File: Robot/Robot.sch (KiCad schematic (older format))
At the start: 3 parts

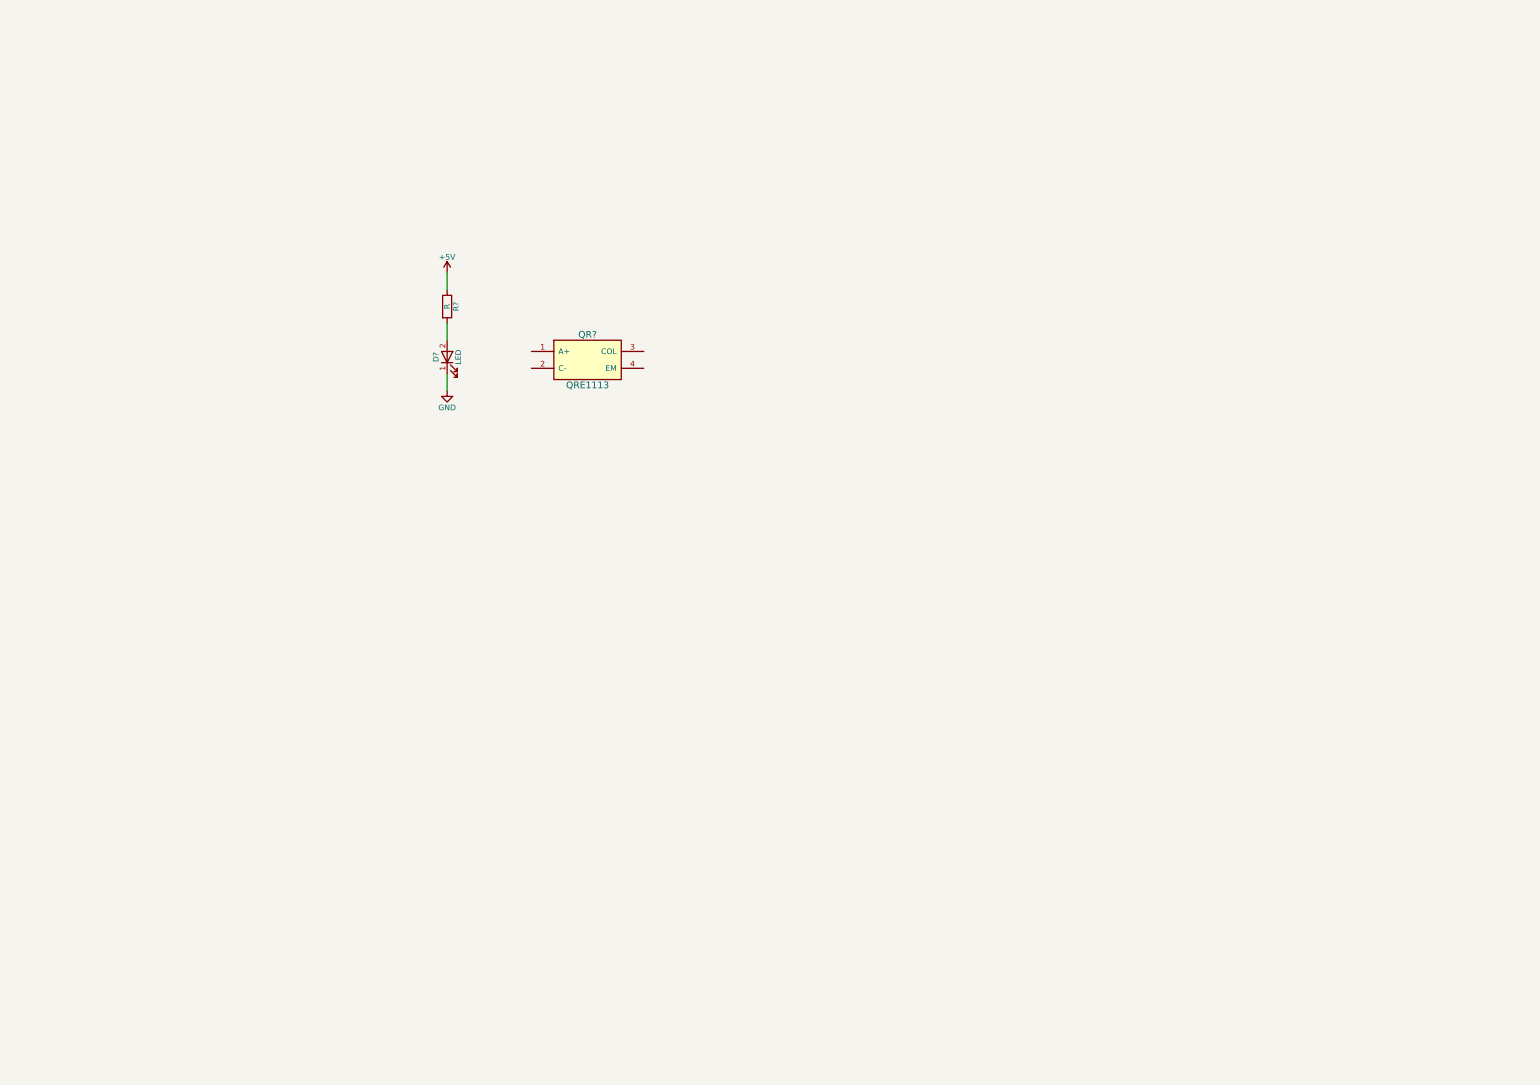
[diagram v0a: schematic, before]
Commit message: Dopolnjena shema za robot.
Dodan krmilnik, senzorji QRE1113, MUX, driver za motorje in enkoderji za
motorje.
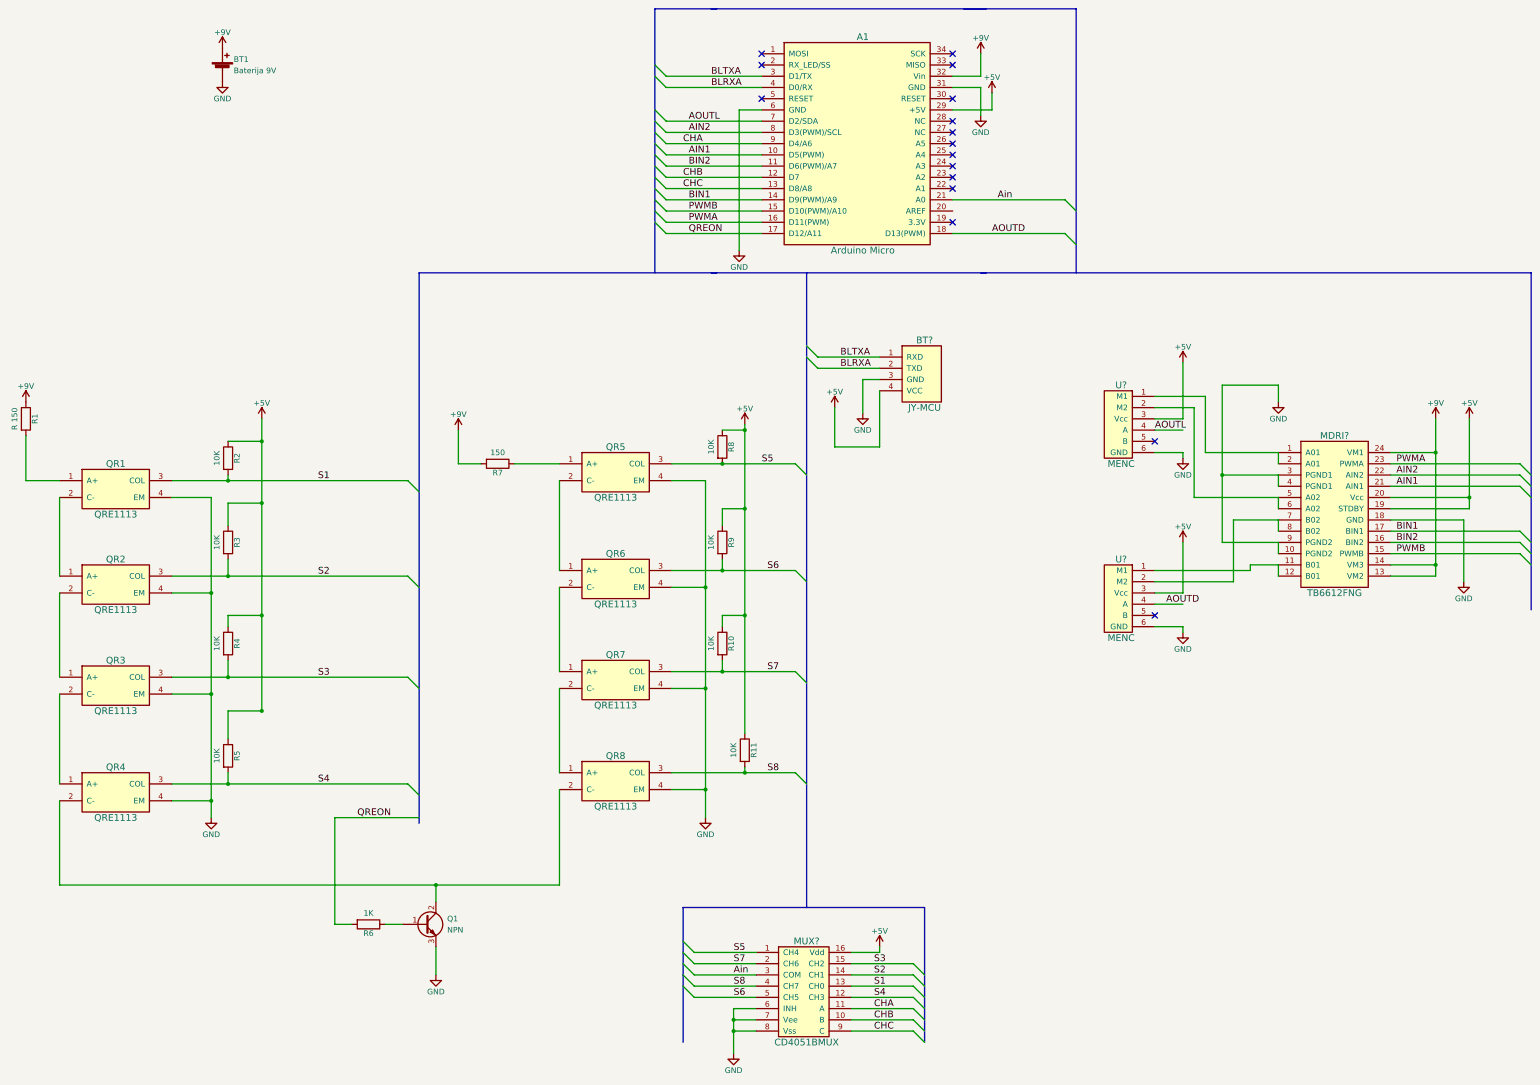
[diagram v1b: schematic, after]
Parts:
- removed D?: LED, symbol LED
- removed QR?: QRE1113, symbol QRE1113
- removed R?: R, symbol R
- added A1: Arduino Micro, symbol arduino-micro
- added BT1: Baterija 9V, symbol Battery_Cell
- added BT?: JY-MCU, symbol JY-MCU
- added MDRI?: TB6612FNG, symbol TB6612FNG
- added MUX?: CD4051BMUX, symbol CD4051BMUX
- added Q1: NPN, symbol Q_NPN_BCE
- added QR1, QR2, QR3, QR4, QR5, QR6, QR7, QR8: QRE1113, symbol QRE1113
- added R1: R 150, symbol R
- added R10, R11, R2, R3, R4, R5, R8, R9: 10K, symbol R
- added R6: 1K, symbol R
- added R7: 150, symbol R
- added U? (x2): MENC, symbol MENC
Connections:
- net +5V: now also A1.29 (+5V), BT?.4 (VCC), MDRI?.19 (STDBY), MDRI?.20 (Vcc), MUX?.16 (Vdd), R10.1, R11.1, R2.1, R3.1, R4.1, R5.1, R8.1, R9.1, U?.3 (Vcc), U?.3 (Vcc)
- net GND: now also A1.31 (GND), A1.6 (GND), BT1.2 (-), BT?.3 (GND), MDRI?.10 (PGND2), MDRI?.18 (GND), MDRI?.3 (PGND1), MDRI?.4 (PGND1), MDRI?.9 (PGND2), MUX?.6 (INH), MUX?.7 (Vee), MUX?.8 (Vss), Q1.3 (E), QR1.4 (EM), QR2.4 (EM), QR3.4 (EM), QR4.4 (EM), QR5.4 (EM), QR6.4 (EM), QR7.4 (EM), QR8.4 (EM), U?.6 (GND), U?.6 (GND)
- new net: QR1.1 (A+), R1.2
- new net: QR1.2 (C-), QR2.1 (A+)
- new net: QR2.2 (C-), QR3.1 (A+)
- new net: QR3.2 (C-), QR4.1 (A+)
- new net: Q1.2 (C), QR4.2 (C-), QR8.2 (C-)
- new net: QR5.1 (A+), R7.1
- new net: QR5.2 (C-), QR6.1 (A+)
- new net: QR6.2 (C-), QR7.1 (A+)
- new net: QR7.2 (C-), QR8.1 (A+)
- new net: Q1.1 (B), R6.1
- new net: MDRI?.1 (A01), MDRI?.2 (A01), U?.1 (M1)
- new net: MDRI?.11 (B01), MDRI?.12 (B01), U?.1 (M1)
- new net: MDRI?.5 (A02), MDRI?.6 (A02), U?.2 (M2)
- new net: MDRI?.7 (B02), MDRI?.8 (B02), U?.2 (M2)
- new net +9V: A1.32 (Vin), BT1.1 (+), MDRI?.13 (VM2), MDRI?.14 (VM3), MDRI?.24 (VM1), R1.1, R7.2
- new net AIN1: A1.10 (D5(PWM)), MDRI?.21 (AIN1)
- new net AIN2: A1.8 (D3(PWM)/SCL), MDRI?.22 (AIN2)
- new net AOUTD: A1.18 (D13(PWM)), U?.4 (A)
- new net AOUTL: A1.7 (D2/SDA), U?.4 (A)
- new net Ain: A1.21 (A0), MUX?.3 (COM)
- new net BIN1: A1.14 (D9(PWM)/A9), MDRI?.17 (BIN1)
- new net BIN2: A1.11 (D6(PWM)/A7), MDRI?.16 (BIN2)
- new net BLRXA: A1.4 (D0/RX), BT?.2 (TXD)
- new net BLTXA: A1.3 (D1/TX), BT?.1 (RXD)
- new net CHA: A1.9 (D4/A6), MUX?.11 (A)
- new net CHB: A1.12 (D7), MUX?.10 (B)
- new net CHC: A1.13 (D8/A8), MUX?.9 (C)
- new net PWMA: A1.16 (D11(PWM)), MDRI?.23 (PWMA)
- new net PWMB: A1.15 (D10(PWM)/A10), MDRI?.15 (PWMB)
- new net QREON: A1.17 (D12/A11), R6.2
- new net S1: MUX?.13 (CH0), QR1.3 (COL), R2.2
- new net S2: MUX?.14 (CH1), QR2.3 (COL), R3.2
- new net S3: MUX?.15 (CH2), QR3.3 (COL), R4.2
- new net S4: MUX?.12 (CH3), QR4.3 (COL), R5.2
- new net S5: MUX?.1 (CH4), QR5.3 (COL), R8.2
- new net S6: MUX?.5 (CH5), QR6.3 (COL), R9.2
- new net S7: MUX?.2 (CH6), QR7.3 (COL), R10.2
- new net S8: MUX?.4 (CH7), QR8.3 (COL), R11.2
- no-connect marks 0 -> 16

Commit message: Dodana povezava B z enkoderjem
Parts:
- added C1, C2: 47uF, symbol C
- gave numbers to parts that had none: 5
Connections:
- net labels added: BOUTD, BOUTL
- wire segments 155 -> 166
- no-connect marks 16 -> 12
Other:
- moved on the sheet: U1
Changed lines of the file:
@@
 $EndComp
 $Comp
-L +9V #PWR8
+L +9V #PWR7
 U 1 1 58BBF0B9
 P 4550 4500
-F 0 "#PWR8" H 4550 4350 50  0001 C CNN
+F 0 "#PWR7" H 4550 4350 50  0001 C CNN
 F 1 "+9V" H 4550 4640 50  0000 C CNN
 F 2 "" H 4550 4500 50  0000 C CNN
@@
 $EndComp
 $Comp
-L GND #PWR6
+L GND #PWR9
 U 1 1 58BC1A56
 P 7000 10050
-F 0 "#PWR6" H 7000 9800 50  0001 C CNN
+F 0 "#PWR9" H 7000 9800 50  0001 C CNN
 F 1 "GND" H 7000 9900 50  0000 C CNN
 F 2 "" H 7000 10050 50  0000 C CNN
@@
 $EndComp
 $Comp
-L GND #PWR12
+L GND #PWR16
 U 1 1 58BC1E52
 P 9200 1700
-F 0 "#PWR12" H 9200 1450 50  0001 C CNN
+F 0 "#PWR16" H 9200 1450 50  0001 C CNN
 F 1 "GND" H 9200 1550 50  0000 C CNN
 F 2 "" H 9200 1700 50  0000 C CNN
@@
 $EndComp
 $Comp
-L +9V #PWR11
+L +9V #PWR15
 U 1 1 58BC1EB1
 P 9200 1150
-F 0 "#PWR11" H 9200 1000 50  0001 C CNN
+F 0 "#PWR15" H 9200 1000 50  0001 C CNN
 F 1 "+9V" H 9200 1290 50  0000 C CNN
 F 2 "" H 9200 1150 50  0000 C CNN
@@
 $EndComp
 $Comp
-L +5V #PWR13
+L +5V #PWR17
 U 1 1 58BC1EDB
 P 9300 1500
-F 0 "#PWR13" H 9300 1350 50  0001 C CNN
+F 0 "#PWR17" H 9300 1350 50  0001 C CNN
 F 1 "+5V" H 9300 1640 50  0000 C CNN
 F 2 "" H 9300 1500 50  0000 C CNN
@@
 $EndComp
 $Comp
-L GND #PWR9
+L GND #PWR10
 U 1 1 58BC1F3F
 P 7050 2900
-F 0 "#PWR9" H 7050 2650 50  0001 C CNN
+F 0 "#PWR10" H 7050 2650 50  0001 C CNN
 F 1 "GND" H 7050 2750 50  0000 C CNN
 F 2 "" H 7050 2900 50  0000 C CNN
@@
 $EndComp
 $Comp
-L +5V #PWR10
+L +5V #PWR11
 U 1 1 58BC95B9
 P 7100 4450
-F 0 "#PWR10" H 7100 4300 50  0001 C CNN
+F 0 "#PWR11" H 7100 4300 50  0001 C CNN
 F 1 "+5V" H 7100 4590 50  0000 C CNN
 F 2 "" H 7100 4450 50  0000 C CNN
@@
 $EndComp
 $Comp
-L GND #PWR7
+L GND #PWR6
 U 1 1 58BCB171
 P 4350 9350
-F 0 "#PWR7" H 4350 9100 50  0001 C CNN
+F 0 "#PWR6" H 4350 9100 50  0001 C CNN
 F 1 "GND" H 4350 9200 50  0000 C CNN
 F 2 "" H 4350 9350 50  0000 C CNN
@@
 	6300 1650 6400 1750
 $Comp
-L CD4051BMUX MUX?
+L CD4051BMUX MUX1
 U 1 1 58BD1AB3
 P 7400 10450
-F 0 "MUX?" H 7650 11850 60  0000 C CNN
+F 0 "MUX1" H 7650 11850 60  0000 C CNN
 F 1 "CD4051BMUX" H 7650 10950 60  0000 C CNN
 F 2 "" H 7400 10450 60  0001 C CNN
@@
 $EndComp
 $Comp
-L GND #PWR?
+L GND #PWR8
 U 1 1 58BD222C
 P 6750 7950
-F 0 "#PWR?" H 6750 7700 50  0001 C CNN
+F 0 "#PWR8" H 6750 7700 50  0001 C CNN
 F 1 "GND" H 6750 7800 50  0000 C CNN
 F 2 "" H 6750 7950 50  0000 C CNN
@@
 S4
 $Comp
-L +5V #PWR?
+L +5V #PWR14
 U 1 1 58BD4C14
 P 8300 9100
-F 0 "#PWR?" H 8300 8950 50  0001 C CNN
+F 0 "#PWR14" H 8300 8950 50  0001 C CNN
 F 1 "+5V" H 8300 9240 50  0000 C CNN
 F 2 "" H 8300 9100 50  0000 C CNN
@@
 	6300 2650 6400 2750
 $Comp
-L JY-MCU BT?
+L JY-MCU BT2
 U 1 1 58BDB3C0
 P 8500 4400
-F 0 "BT?" H 8700 5100 60  0000 C CNN
+F 0 "BT2" H 8700 5100 60  0000 C CNN
 F 1 "JY-MCU" H 8700 4500 60  0000 C CNN
 F 2 "" H 8500 4400 60  0001 C CNN
@@
 BLRXA
 $Comp
-L GND #PWR?
+L GND #PWR13
 U 1 1 58BDD562
 P 8150 4350
-F 0 "#PWR?" H 8150 4100 50  0001 C CNN
+F 0 "#PWR13" H 8150 4100 50  0001 C CNN
 F 1 "GND" H 8150 4200 50  0000 C CNN
 F 2 "" H 8150 4350 50  0000 C CNN
@@
 $EndComp
 $Comp
-L +5V #PWR?
+L +5V #PWR12
 U 1 1 58BDD71C
 P 7900 4300
-F 0 "#PWR?" H 7900 4150 50  0001 C CNN
+F 0 "#PWR12" H 7900 4150 50  0001 C CNN
 F 1 "+5V" H 7900 4440 50  0000 C CNN
 F 2 "" H 7900 4300 50  0000 C CNN
@@
 NoConn ~ 8950 2650
 $Comp
-L TB6612FNG MDRI?
+L TB6612FNG MDRI1
 U 1 1 58BDF07E
 P 11850 5950
-F 0 "MDRI?" H 12350 7350 60  0000 C CNN
+F 0 "MDRI1" H 12350 7350 60  0000 C CNN
 F 1 "TB6612FNG" H 12350 5950 60  0000 C CNN
 F 2 "" H 11850 5950 60  0001 C CNN
@@
 $EndComp
 $Comp
-L +9V #PWR?
+L +9V #PWR23
 U 1 1 58BDF7BA
 P 13250 4400
-F 0 "#PWR?" H 13250 4250 50  0001 C CNN
+F 0 "#PWR23" H 13250 4250 50  0001 C CNN
 F 1 "+9V" H 13250 4540 50  0000 C CNN
 F 2 "" H 13250 4400 50  0000 C CNN
@@
 $EndComp
 $Comp
-L GND #PWR?
+L GND #PWR24
 U 1 1 58BDF8AC
 P 13500 5850
-F 0 "#PWR?" H 13500 5600 50  0001 C CNN
+F 0 "#PWR24" H 13500 5600 50  0001 C CNN
 F 1 "GND" H 13500 5700 50  0000 C CNN
 F 2 "" H 13500 5850 50  0000 C CNN
@@
 $EndComp
 $Comp
-L MENC U?
+L MENC U1
 U 1 1 58BE0D00
-P 10000 4950
-F 0 "U?" H 10450 5800 60  0000 C CNN
-F 1 "MENC" H 10450 5100 60  0000 C CNN
-F 2 "" H 10250 5250 60  0001 C CNN
-F 3 "" H 10250 5250 60  0001 C CNN
-	1    10000 4950
-	1    0    0    -1
-$EndComp
-$Comp
-L MENC U?
+P 9750 4950
+F 0 "U1" H 10200 5800 60  0000 C CNN
+F 1 "MENC" H 10200 5100 60  0000 C CNN
+F 2 "" H 10000 5250 60  0001 C CNN
+F 3 "" H 10000 5250 60  0001 C CNN
+	1    9750 4950
+	1    0    0    -1
+$EndComp
+$Comp
+L MENC U2
 U 1 1 58BE0DEF
 P 10000 6500
-F 0 "U?" H 10450 7350 60  0000 C CNN
+F 0 "U2" H 10450 7350 60  0000 C CNN
 F 1 "MENC" H 10450 6650 60  0000 C CNN
 F 2 "" H 10250 6800 60  0001 C CNN
@@
 $EndComp
 $Comp
-L +5V #PWR?
+L +5V #PWR20
 U 1 1 58BE122F
 P 11000 5500
-F 0 "#PWR?" H 11000 5350 50  0001 C CNN
+F 0 "#PWR20" H 11000 5350 50  0001 C CNN
 F 1 "+5V" H 11000 5640 50  0000 C CNN
 F 2 "" H 11000 5500 50  0000 C CNN
@@
 $EndComp
 $Comp
-L +5V #PWR?
+L +5V #PWR18
 U 1 1 58BE1351
-P 11000 3900
-F 0 "#PWR?" H 11000 3750 50  0001 C CNN
-F 1 "+5V" H 11000 4040 50  0000 C CNN
-F 2 "" H 11000 3900 50  0000 C CNN
-F 3 "" H 11000 3900 50  0000 C CNN
-	1    11000 3900
-	1    0    0    -1
-$EndComp
-$Comp
-L GND #PWR?
+P 10750 3900
+F 0 "#PWR18" H 10750 3750 50  0001 C CNN
+F 1 "+5V" H 10750 4040 50  0000 C CNN
+F 2 "" H 10750 3900 50  0000 C CNN
+F 3 "" H 10750 3900 50  0000 C CNN
+	1    10750 3900
+	1    0    0    -1
+$EndComp
+$Comp
+L GND #PWR21
 U 1 1 58BE1697
 P 11000 6300
-F 0 "#PWR?" H 11000 6050 50  0001 C CNN
+F 0 "#PWR21" H 11000 6050 50  0001 C CNN
 F 1 "GND" H 11000 6150 50  0000 C CNN
 F 2 "" H 11000 6300 50  0000 C CNN
@@
 $EndComp
 $Comp
-L GND #PWR?
+L GND #PWR19
 U 1 1 58BE16E1
-P 11000 4750
-F 0 "#PWR?" H 11000 4500 50  0001 C CNN
-F 1 "GND" H 11000 4600 50  0000 C CNN
-F 2 "" H 11000 4750 50  0000 C CNN
-F 3 "" H 11000 4750 50  0000 C CNN
-	1    11000 4750
-	1    0    0    -1
-$EndComp
-$Comp
-L GND #PWR?
+P 10750 4750
+F 0 "#PWR19" H 10750 4500 50  0001 C CNN
+F 1 "GND" H 10750 4600 50  0000 C CNN
+F 2 "" H 10750 4750 50  0000 C CNN
+F 3 "" H 10750 4750 50  0000 C CNN
+	1    10750 4750
+	1    0    0    -1
+$EndComp
+$Comp
+L GND #PWR22
 U 1 1 58BE195D
 P 11850 4250
-F 0 "#PWR?" H 11850 4000 50  0001 C CNN
+F 0 "#PWR22" H 11850 4000 50  0001 C CNN
 F 1 "GND" H 11850 4100 50  0000 C CNN
 F 2 "" H 11850 4250 50  0000 C CNN
@@
 $EndComp
 $Comp
-L +5V #PWR?
+L +5V #PWR25
 U 1 1 58BE1A8C
 P 13550 4400
-F 0 "#PWR?" H 13550 4250 50  0001 C CNN
+F 0 "#PWR25" H 13550 4250 50  0001 C CNN
 F 1 "+5V" H 13550 4540 50  0000 C CNN
 F 2 "" H 13550 4400 50  0000 C CNN
@@
 NoConn ~ 8950 2050
 NoConn ~ 8950 2150
-NoConn ~ 8950 2250
-NoConn ~ 8950 2350
 Entry Wire Line
 	9950 2750 10050 2850
@@
 Text Label 12900 5500 0    60   ~ 0
 BIN2
-NoConn ~ 10750 6150
-NoConn ~ 10750 4600
 Text Label 6600 2650 0    60   ~ 0
 PWMA
@@
 Text Label 9300 2750 0    60   ~ 0
 AOUTD
-Text Label 10750 4500 0    60   ~ 0
+Text Label 10500 4500 0    60   ~ 0
 AOUTL
 Text Label 10850 6050 0    60   ~ 0
@@
 	11450 5300 11850 5300
 Wire Wire Line
-	11100 5100 11850 5100
+	10850 5100 11850 5100
 Wire Wire Line
 	11350 4900 11850 4900
 Wire Wire Line
-	11200 4700 11850 4700
-Wire Wire Line
-	10750 4400 11000 4400
-Wire Wire Line
-	11000 4400 11000 3900
+	10950 4700 11850 4700
+Wire Wire Line
+	10500 4400 10750 4400
+Wire Wire Line
+	10750 4400 10750 3900
 Wire Wire Line
 	10750 5950 11000 5950
@@
 	11000 5950 11000 5500
 Wire Wire Line
-	10750 4700 11000 4700
-Wire Wire Line
-	11000 4700 11000 4750
+	10500 4700 10750 4700
+Wire Wire Line
+	10750 4700 10750 4750
 Wire Wire Line
 	10750 6250 11000 6250
@@
 	12850 5100 13550 5100
 Wire Wire Line
-	11200 4700 11200 4200
-Wire Wire Line
-	11200 4200 10750 4200
-Wire Wire Line
-	11100 5100 11100 4300
-Wire Wire Line
-	11100 4300 10750 4300
+	10500 4200 10950 4200
+Wire Wire Line
+	10850 4300 10500 4300
 Wire Wire Line
 	11600 5700 11600 5750
@@
 	8950 2750 9950 2750
 Wire Wire Line
-	10750 4500 11000 4500
+	10500 4500 10750 4500
 Wire Wire Line
 	10750 6050 11000 6050
+Wire Wire Line
+	10850 5100 10850 4300
+$Comp
+L C C1
+U 1 1 58BC6218
+P 11050 4900
+F 0 "C1" H 11075 5000 50  0000 L CNN
+F 1 "47uF" H 11075 4800 50  0000 L CNN
+F 2 "" H 11088 4750 50  0000 C CNN
+F 3 "" H 11050 4900 50  0000 C CNN
+	1    11050 4900
+	1    0    0    -1
+$EndComp
+Wire Wire Line
+	10950 4200 10950 4700
+Wire Wire Line
+	11050 4750 11050 4700
+Connection ~ 11050 4700
+Wire Wire Line
+	11050 5050 11050 5100
+Connection ~ 11050 5100
+$Comp
+L C C2
+U 1 1 58BC6B76
+P 11350 6300
+F 0 "C2" H 11375 6400 50  0000 L CNN
+F 1 "47uF" H 11375 6200 50  0000 L CNN
+F 2 "" H 11388 6150 50  0000 C CNN
+F 3 "" H 11350 6300 50  0000 C CNN
+	1    11350 6300
+	0    -1   -1   0
+$EndComp
+Wire Wire Line
+	11200 5850 11200 6300
+Connection ~ 11200 5850
+Wire Wire Line
+	11400 5750 11400 6000
+Wire Wire Line
+	11400 6000 11600 6000
+Wire Wire Line
+	11600 6000 11600 6300
+Wire Wire Line
+	11600 6300 11500 6300
+Connection ~ 11400 5750
+Wire Wire Line
+	10750 6150 11050 6150
+Wire Wire Line
+	10500 4600 10750 4600
+Text Label 10500 4600 0    60   ~ 0
+BOUTL
+Text Label 9050 2350 0    60   ~ 0
+BOUTL
+Text Label 9050 2250 0    60   ~ 0
+BOUTD
+Text Label 10850 6150 0    60   ~ 0
+BOUTD
+Wire Wire Line
+	8950 2250 9350 2250
+Wire Wire Line
+	8950 2350 9350 2350
 $EndSCHEMATC
